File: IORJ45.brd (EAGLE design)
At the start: 73.7 x 40.6 mm, 19 parts, among them J3 RJ45-8X44UCON19514

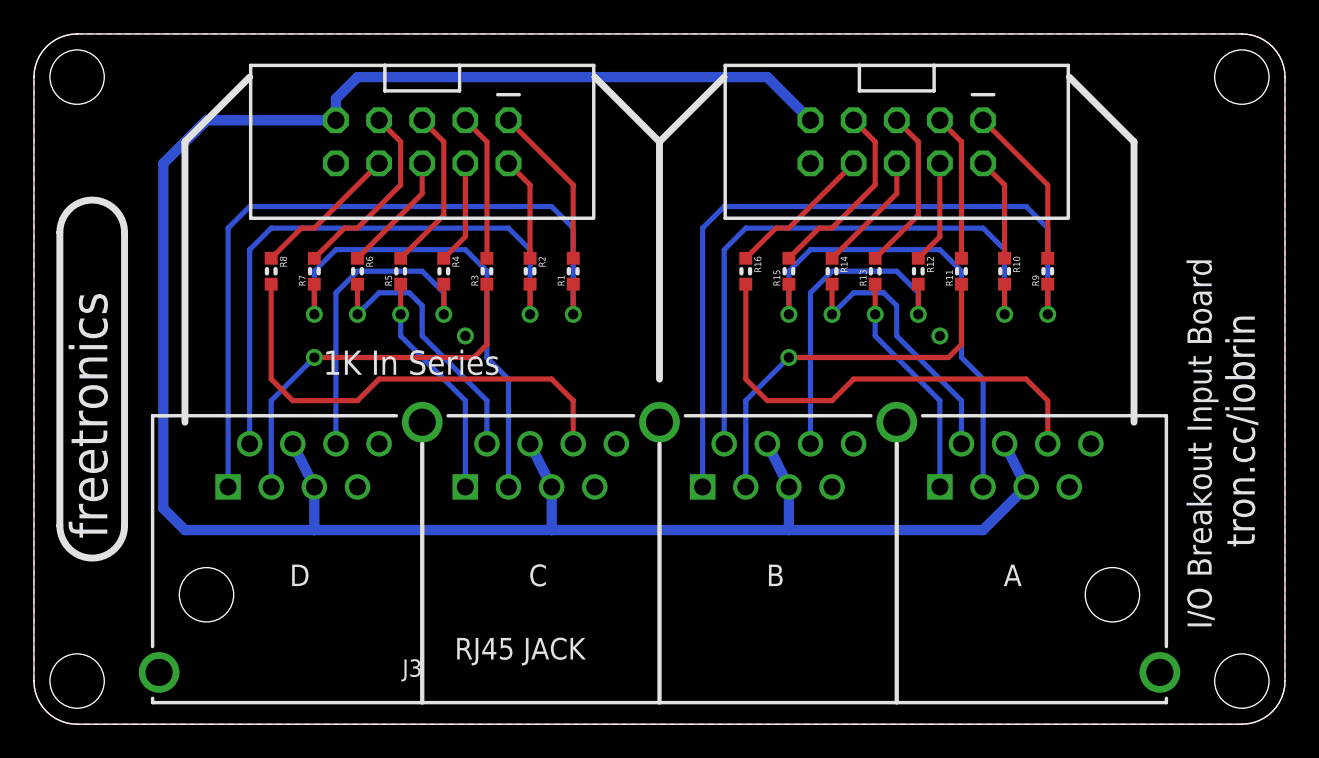
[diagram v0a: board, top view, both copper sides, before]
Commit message: Converted to 2x6 header for v2.0 release
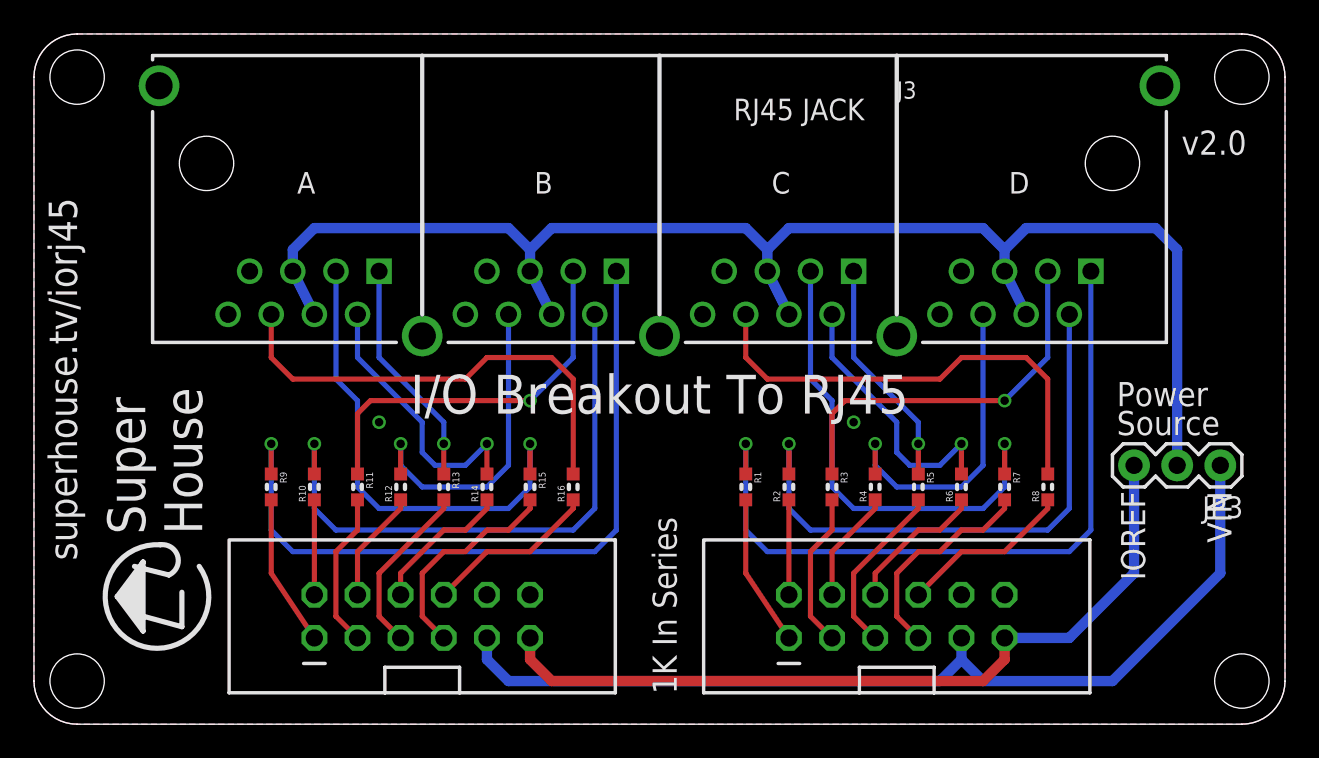
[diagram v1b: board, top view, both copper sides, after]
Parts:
- added JP3: POWER, freetronics-jon:1X03
- J3: device freetronics-2:RJ45-8X4 -> freetronics-jon:RJ45-8X4
- JP1, JP2: value M05X2SHD -> M06X2; device freetronics-original:2X5-SHROUDED -> freetronics-jon:2X6-SHROUDED
- moved R8 47.5 mm to (59.7, 14.0), turned to 90 degrees
- moved R9 47.5 mm to (14.0, 14.0), turned to 270 degrees
- moved JP2 45.0 mm to (16.5, 5.08), turned to 90 degrees
- moved R10 42.6 mm to (16.5, 14.0), turned to 90 degrees
- moved R7 42.6 mm to (57.1, 14.0), turned to 270 degrees
- moved R11 37.8 mm to (19.1, 14.0), turned to 270 degrees
- moved R6 37.8 mm to (54.6, 14.0), turned to 90 degrees
- moved JP1 36.3 mm to (44.5, 5.08), turned to 90 degrees
- moved R12 33.0 mm to (21.6, 14.0), turned to 90 degrees
- moved R5 33.0 mm to (52.1, 14.0), turned to 270 degrees
- moved R13 28.4 mm to (24.1, 14.0), turned to 270 degrees
- moved R4 28.4 mm to (49.5, 14.0), turned to 90 degrees
- moved J3 25.4 mm to (36.8, 33.0), turned to 0 degrees
- moved R14 24.0 mm to (26.7, 14.0), turned to 90 degrees
- moved R3 24.0 mm to (47.0, 14.0), turned to 270 degrees
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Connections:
- net A6 renamed A4
- net B6 renamed B4
- net C6 renamed C4
- net D6 renamed D4
- new net IOREF: JP1.11, JP2.11, JP3.3
- new net RESET1: JP1.12
- new net RESET2: JP2.12
- new net VIN: JP1.9, JP2.9, JP3.1
- net VCC: now also JP3.2; no longer JP1.9, JP2.9
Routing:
- net VIN: track 0.00 -> 56.3 mm
- net VCC: track 133.7 -> 85.4 mm
- net IOREF: track 0.00 -> 47.1 mm
- net N$5: track 11.2 -> 12.8 mm
- net N$16: track 8.66 -> 10.2 mm
- net N$12: track 11.2 -> 12.8 mm
- net N$8: track 8.66 -> 10.2 mm
- net N$15: track 7.17 -> 8.44 mm
- net N$9: track 7.17 -> 8.44 mm
- net N$7: track 9.71 -> 8.90 mm
- net N$4: track 9.71 -> 8.90 mm
- net N$2: track 9.71 -> 10.2 mm
- net N$11: track 6.11 -> 5.59 mm
- net N$18: track 6.11 -> 5.59 mm
- net N$6: track 8.65 -> 9.18 mm
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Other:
- board text added: "(C)2017 SuperHouse Automation Pty Ltd Licensed under the TAPR Open Hardware License www.tapr.org/OHL"
- board text added: "1"
- board text added: "2"
- board text added: "3"
- board text added: "4"
- board text added: "5"
- board text added: "6"
- board text added: "7"
- board text added: "8"
- board text added: "GND"
- board text added: "I/O Breakout To RJ45"
- board text added: "IOREF"
- board text added: "Power Source"
- board text added: "RESET"
- board text added: "SKU: IORJ45"
- board text added: "Super House"
- board text added: "VIN"
- board text added: "superhouse.tv/iorj45"
- board text added: "v2.0"
- board text removed: "(C)2014 SuperHouse Pty Ltd"
- board text removed: "I/O Breakout Input Board"
- board text removed: "SKU: IOBRIN"
- board text removed: "freetronics"
- board text removed: "tron.cc/iobrin"
- board text removed: "v1.0"
- board text removed: "www.freetronics.com/iobrin"

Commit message: Part replacement using SuperHouse libraries
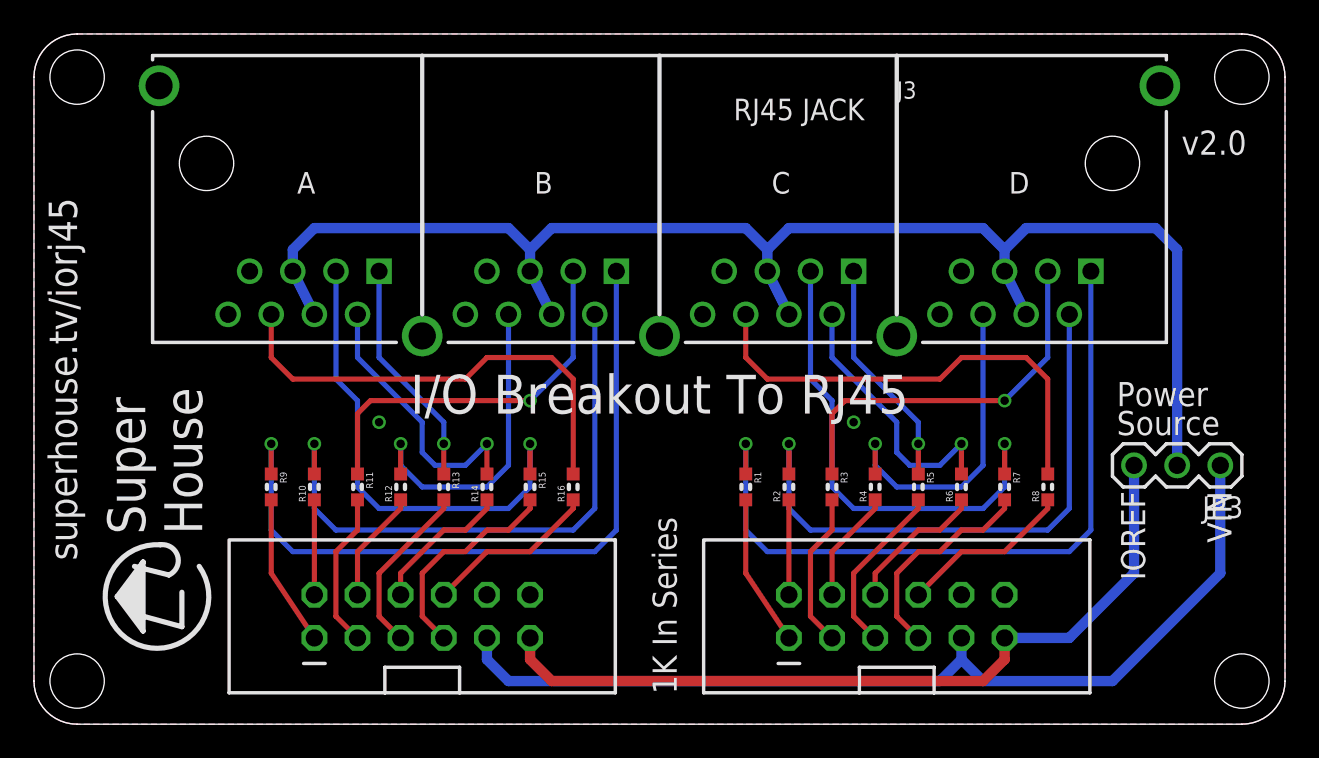
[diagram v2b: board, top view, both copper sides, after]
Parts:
- J3: device freetronics-jon:RJ45-8X4 -> SuperHouse-Connectors:RJ45-8X4
- JP1, JP2: value M06X2 -> M06X2-SHROUDED; device freetronics-jon:2X6-SHROUDED -> SuperHouse-Connectors:2X6-SHROUDED
- JP3: device freetronics-jon:1X03 -> SuperHouse-Connectors:1X03-P
- R1, R10, R11, R12, R13, R14, R15, R16, R2, R3, R4, R5, R6, R7, R8, R9: device freetronics-jon:0603 -> SuperHouse-DiscreteSemi:R0603
